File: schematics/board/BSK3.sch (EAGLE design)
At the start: 27 parts

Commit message: Платы подготовлены для Резонита
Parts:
- removed U$14: FS8205A, CanCubeSat:FS8205A
- added FS8205A: FS8205A+, CanCubeSat:FS8205A+
- renumbered U$5 to DS18B20Z, U$8 to L293DD
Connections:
- net BUS-: now also FS8205A.S1; no longer U$14.S1
- net GND: now also FS8205A.S2; no longer U$14.S2
- net HEAT: now also FS8205A.HEAT; no longer U$14.HEAT
- net N$8: now also FS8205A.G1; no longer U$14.G1
- net N$9: now also FS8205A.G2; no longer U$14.G2
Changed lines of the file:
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@@
 </classes>
 <parts>
-<part name="U$5" library="CanCubeSat" deviceset="DS18B20Z" device=""/>
+<part name="DS18B20Z" library="CanCubeSat" deviceset="DS18B20Z" device=""/>
 <part name="U$6" library="CanCubeSat" deviceset="EM_HEAT" device=""/>
 <part name="U$7" library="CanCubeSat" deviceset="EM_HEAT" device=""/>
-<part name="U$8" library="CanCubeSat" deviceset="L293DD" device=""/>
-<part name="U$14" library="CanCubeSat" deviceset="FS8205A" device=""/>
+<part name="L293DD" library="CanCubeSat" deviceset="L293DD" device=""/>
+<part name="FS8205A" library="CanCubeSat" deviceset="FS8205A+" device=""/>
 <part name="R10" library="resistor" library_urn="urn:adsk.eagle:library:348" deviceset="R-US_" device="R0603" package3d_urn="urn:adsk.eagle:package:23555/3" value="10k"/>
 <part name="R11" library="resistor" library_urn="urn:adsk.eagle:library:348" deviceset="R-US_" device="R0603" package3d_urn="urn:adsk.eagle:package:23555/3" value="10k"/>
@@
 </plain>
 <instances>
-<instance part="U$5" gate="G$1" x="119.38" y="160.02" smashed="yes"/>
+<instance part="DS18B20Z" gate="G$1" x="119.38" y="160.02" smashed="yes"/>
 <instance part="U$6" gate="G$1" x="55.88" y="231.14" smashed="yes" rot="R90"/>
 <instance part="U$7" gate="G$1" x="71.12" y="231.14" smashed="yes" rot="R270"/>
-<instance part="U$8" gate="G$1" x="63.5" y="203.2" smashed="yes" rot="R270"/>
-<instance part="U$14" gate="G$1" x="162.56" y="215.9" smashed="yes"/>
+<instance part="L293DD" gate="G$1" x="63.5" y="203.2" smashed="yes" rot="R270"/>
+<instance part="FS8205A" gate="G$1" x="162.56" y="215.9" smashed="yes"/>
 <instance part="R10" gate="G$1" x="157.48" y="233.68" smashed="yes" rot="R270">
 <attribute name="NAME" x="158.9786" y="237.49" size="1.778" layer="95" rot="R270"/>
@@
 </segment>
 <segment>
-<pinref part="U$5" gate="G$1" pin="GND"/>
+<pinref part="DS18B20Z" gate="G$1" pin="GND"/>
 <wire x1="129.54" y1="157.48" x2="137.16" y2="157.48" width="0.1524" layer="91"/>
 <label x="130.556" y="157.48" size="1.778" layer="95"/>
 </segment>
 <segment>
-<pinref part="U$8" gate="G$1" pin="GND"/>
+<pinref part="L293DD" gate="G$1" pin="GND"/>
 <wire x1="50.8" y1="205.74" x2="38.1" y2="205.74" width="0.1524" layer="91"/>
 <label x="39.116" y="205.74" size="1.778" layer="95"/>
 </segment>
 <segment>
-<pinref part="U$14" gate="G$1" pin="S2"/>
+<pinref part="FS8205A" gate="G$1" pin="S2"/>
 <wire x1="175.26" y1="215.9" x2="185.42" y2="215.9" width="0.1524" layer="91"/>
 <label x="180.34" y="215.9" size="1.778" layer="95"/>
@@
 <net name="5V" class="0">
 <segment>
-<pinref part="U$8" gate="G$1" pin="EN1"/>
+<pinref part="L293DD" gate="G$1" pin="EN1"/>
 <wire x1="50.8" y1="213.36" x2="38.1" y2="213.36" width="0.1524" layer="91"/>
 <label x="38.862" y="213.36" size="1.778" layer="95"/>
 </segment>
 <segment>
-<pinref part="U$8" gate="G$1" pin="VS"/>
+<pinref part="L293DD" gate="G$1" pin="VS"/>
 <wire x1="50.8" y1="190.5" x2="38.1" y2="190.5" width="0.1524" layer="91"/>
 <label x="38.862" y="190.5" size="1.778" layer="95"/>
 </segment>
 <segment>
-<pinref part="U$8" gate="G$1" pin="EN2"/>
+<pinref part="L293DD" gate="G$1" pin="EN2"/>
 <wire x1="76.2" y1="190.5" x2="81.28" y2="190.5" width="0.1524" layer="91"/>
 <label x="77.47" y="190.5" size="1.778" layer="95"/>
 </segment>
 <segment>
-<pinref part="U$8" gate="G$1" pin="VSS"/>
+<pinref part="L293DD" gate="G$1" pin="VSS"/>
 <wire x1="76.2" y1="213.36" x2="81.28" y2="213.36" width="0.1524" layer="91"/>
 <label x="77.216" y="213.36" size="1.778" layer="95"/>
@@
 </segment>
 <segment>
-<pinref part="U$5" gate="G$1" pin="VDD"/>
+<pinref part="DS18B20Z" gate="G$1" pin="VDD"/>
 <wire x1="106.68" y1="160.02" x2="99.06" y2="160.02" width="0.1524" layer="91"/>
 <label x="101.6" y="160.02" size="1.778" layer="95"/>
@@
 <net name="1W" class="0">
 <segment>
-<pinref part="U$5" gate="G$1" pin="DQ"/>
+<pinref part="DS18B20Z" gate="G$1" pin="DQ"/>
 <wire x1="106.68" y1="157.48" x2="99.06" y2="157.48" width="0.1524" layer="91"/>
 <label x="101.6" y="157.48" size="1.778" layer="95"/>
@@
 </segment>
 <segment>
-<pinref part="U$8" gate="G$1" pin="IN1"/>
+<pinref part="L293DD" gate="G$1" pin="IN1"/>
 <wire x1="50.8" y1="210.82" x2="38.1" y2="210.82" width="0.1524" layer="91"/>
 <label x="38.862" y="210.82" size="1.778" layer="95"/>
@@
 </segment>
 <segment>
-<pinref part="U$8" gate="G$1" pin="IN2"/>
+<pinref part="L293DD" gate="G$1" pin="IN2"/>
 <wire x1="50.8" y1="193.04" x2="38.1" y2="193.04" width="0.1524" layer="91"/>
 <label x="38.862" y="193.04" size="1.778" layer="95"/>
@@
 </segment>
 <segment>
-<pinref part="U$8" gate="G$1" pin="IN4"/>
+<pinref part="L293DD" gate="G$1" pin="IN4"/>
 <wire x1="76.2" y1="210.82" x2="86.36" y2="210.82" width="0.1524" layer="91"/>
 <label x="76.962" y="210.82" size="1.778" layer="95"/>
@@
 <wire x1="35.56" y1="228.6" x2="30.48" y2="228.6" width="0.1524" layer="91"/>
 <wire x1="30.48" y1="228.6" x2="30.48" y2="208.28" width="0.1524" layer="91"/>
-<pinref part="U$8" gate="G$1" pin="OUT1"/>
+<pinref part="L293DD" gate="G$1" pin="OUT1"/>
 <wire x1="30.48" y1="208.28" x2="50.8" y2="208.28" width="0.1524" layer="91"/>
 <pinref part="LED2" gate="G$1" pin="A"/>
@@
 <segment>
 <wire x1="27.94" y1="246.38" x2="27.94" y2="195.58" width="0.1524" layer="91"/>
-<pinref part="U$8" gate="G$1" pin="OUT2"/>
+<pinref part="L293DD" gate="G$1" pin="OUT2"/>
 <wire x1="27.94" y1="195.58" x2="50.8" y2="195.58" width="0.1524" layer="91"/>
 <pinref part="U$6" gate="G$1" pin="GND"/>
@@
 <segment>
 <wire x1="101.6" y1="246.38" x2="101.6" y2="208.28" width="0.1524" layer="91"/>
-<pinref part="U$8" gate="G$1" pin="OUT4"/>
+<pinref part="L293DD" gate="G$1" pin="OUT4"/>
 <wire x1="101.6" y1="208.28" x2="76.2" y2="208.28" width="0.1524" layer="91"/>
 <pinref part="U$7" gate="G$1" pin="5V"/>
@@
 <net name="BUS-" class="0">
 <segment>
-<pinref part="U$14" gate="G$1" pin="S1"/>
+<pinref part="FS8205A" gate="G$1" pin="S1"/>
 <wire x1="142.24" y1="215.9" x2="149.86" y2="215.9" width="0.1524" layer="91"/>
 <pinref part="R20" gate="G$1" pin="2"/>
@@
 <net name="N$8" class="0">
 <segment>
-<pinref part="U$14" gate="G$1" pin="G1"/>
+<pinref part="FS8205A" gate="G$1" pin="G1"/>
 <pinref part="R10" gate="G$1" pin="2"/>
 <wire x1="157.48" y1="228.6" x2="157.48" y2="226.06" width="0.1524" layer="91"/>
@@
 <pinref part="R11" gate="G$1" pin="2"/>
 <wire x1="167.64" y1="228.6" x2="167.64" y2="226.06" width="0.1524" layer="91"/>
-<pinref part="U$14" gate="G$1" pin="G2"/>
+<pinref part="FS8205A" gate="G$1" pin="G2"/>
 </segment>
 </net>
@@
 <net name="HEAT" class="0">
 <segment>
-<pinref part="U$8" gate="G$1" pin="HEAT"/>
+<pinref part="L293DD" gate="G$1" pin="HEAT"/>
 <wire x1="53.34" y1="200.66" x2="35.56" y2="200.66" width="0.1524" layer="91"/>
 <wire x1="35.56" y1="200.66" x2="35.56" y2="180.34" width="0.1524" layer="91"/>
 <wire x1="35.56" y1="180.34" x2="127" y2="180.34" width="0.1524" layer="91"/>
-<pinref part="U$5" gate="G$1" pin="HEAT"/>
+<pinref part="DS18B20Z" gate="G$1" pin="HEAT"/>
 <wire x1="127" y1="180.34" x2="127" y2="162.56" width="0.1524" layer="91"/>
-<pinref part="U$14" gate="G$1" pin="HEAT"/>
+<pinref part="FS8205A" gate="G$1" pin="HEAT"/>
 <wire x1="162.56" y1="208.28" x2="162.56" y2="180.34" width="0.1524" layer="91"/>
 <wire x1="162.56" y1="180.34" x2="127" y2="180.34" width="0.1524" layer="91"/>

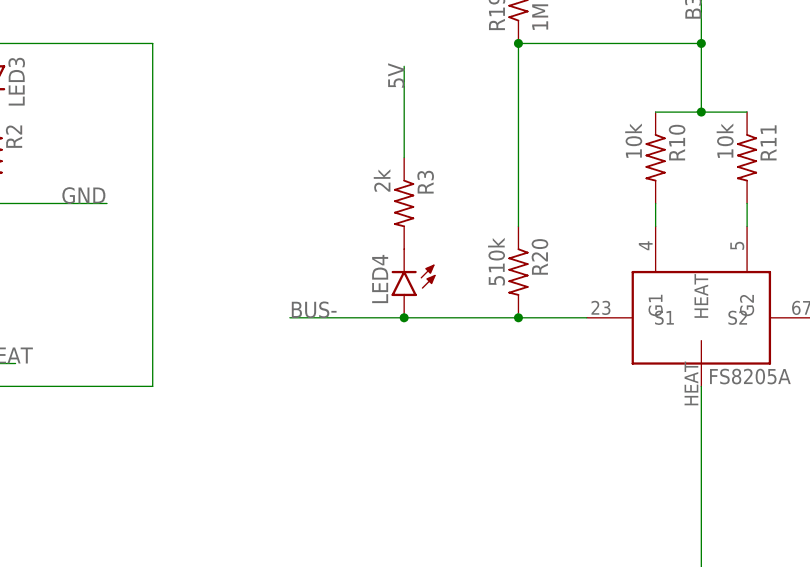
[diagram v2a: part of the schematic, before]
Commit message: Исправлены RADIO и диоды
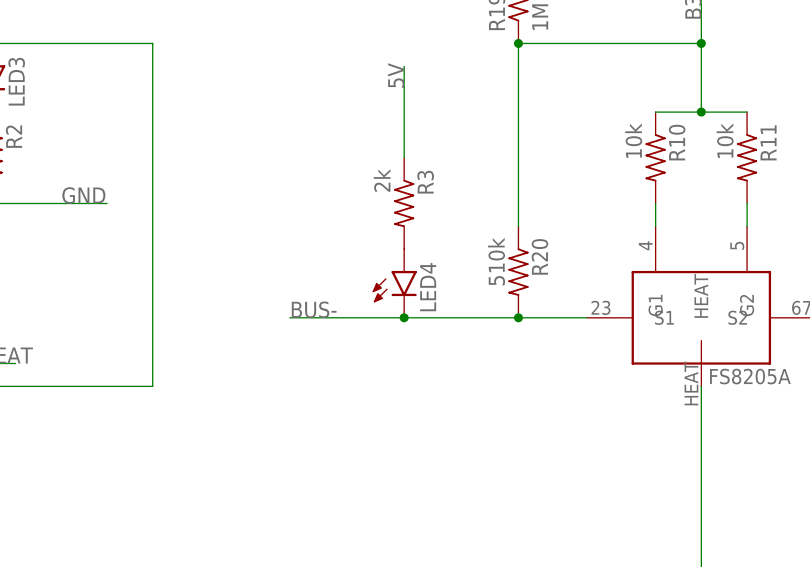
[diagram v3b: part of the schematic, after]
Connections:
- net BUS-: now also LED4.C; no longer LED4.A
- net N$7: now also LED4.A; no longer LED4.C
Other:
- moved on the sheet: LED4
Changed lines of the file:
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@@
 <part name="R2" library="resistor" library_urn="urn:adsk.eagle:library:348" deviceset="R-US_" device="R0603" package3d_urn="urn:adsk.eagle:package:23555/3" value="2k"/>
 <part name="LED3" library="led" library_urn="urn:adsk.eagle:library:259" deviceset="LED" device="CHIPLED_0603" package3d_urn="urn:adsk.eagle:package:15822/2"/>
+<part name="R3" library="resistor" library_urn="urn:adsk.eagle:library:348" deviceset="R-US_" device="R0603" package3d_urn="urn:adsk.eagle:package:23555/3" value="2k"/>
 <part name="LED4" library="led" library_urn="urn:adsk.eagle:library:259" deviceset="LED" device="CHIPLED_0603" package3d_urn="urn:adsk.eagle:package:15822/2"/>
-<part name="R3" library="resistor" library_urn="urn:adsk.eagle:library:348" deviceset="R-US_" device="R0603" package3d_urn="urn:adsk.eagle:package:23555/3" value="2k"/>
 </parts>
 <sheets>
@@
 <attribute name="VALUE" x="89.535" y="239.268" size="1.778" layer="96" rot="R90"/>
 </instance>
-<instance part="LED4" gate="G$1" x="129.54" y="218.44" smashed="yes" rot="R180">
-<attribute name="NAME" x="125.984" y="223.012" size="1.778" layer="95" rot="R270"/>
-<attribute name="VALUE" x="123.825" y="223.012" size="1.778" layer="96" rot="R270"/>
-</instance>
 <instance part="R3" gate="G$1" x="129.54" y="228.6" smashed="yes" rot="R270">
 <attribute name="NAME" x="131.0386" y="232.41" size="1.778" layer="95" rot="R270"/>
 <attribute name="VALUE" x="126.238" y="232.41" size="1.778" layer="96" rot="R270"/>
+</instance>
+<instance part="LED4" gate="G$1" x="129.54" y="220.98" smashed="yes">
+<attribute name="NAME" x="133.096" y="216.408" size="1.778" layer="95" rot="R90"/>
+<attribute name="VALUE" x="135.255" y="216.408" size="1.778" layer="96" rot="R90"/>
 </instance>
 </instances>
@@
 <wire x1="142.24" y1="215.9" x2="149.86" y2="215.9" width="0.1524" layer="91"/>
 <pinref part="R20" gate="G$1" pin="2"/>
-<wire x1="142.24" y1="215.9" x2="129.54" y2="215.9" width="0.1524" layer="91"/>
 <junction x="142.24" y="215.9"/>
 <label x="116.84" y="215.9" size="1.778" layer="95"/>
-<pinref part="LED4" gate="G$1" pin="A"/>
+<wire x1="142.24" y1="215.9" x2="129.54" y2="215.9" width="0.1524" layer="91"/>
+<pinref part="LED4" gate="G$1" pin="C"/>
 <wire x1="129.54" y1="215.9" x2="116.84" y2="215.9" width="0.1524" layer="91"/>
 <junction x="129.54" y="215.9"/>
@@
 <net name="N$7" class="0">
 <segment>
+<pinref part="LED4" gate="G$1" pin="A"/>
 <pinref part="R3" gate="G$1" pin="2"/>
-<pinref part="LED4" gate="G$1" pin="C"/>
-</segment>
-</net>
+</segment>
+</net>

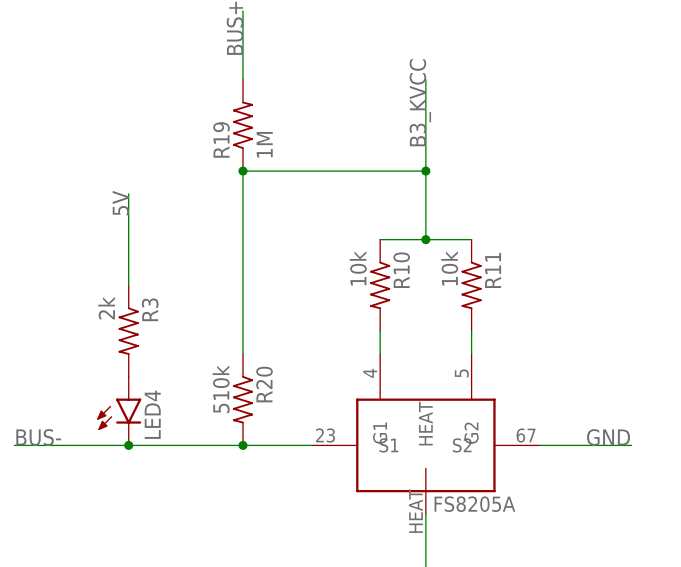
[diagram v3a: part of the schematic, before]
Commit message: Резисторы у FS8205A 100Ом
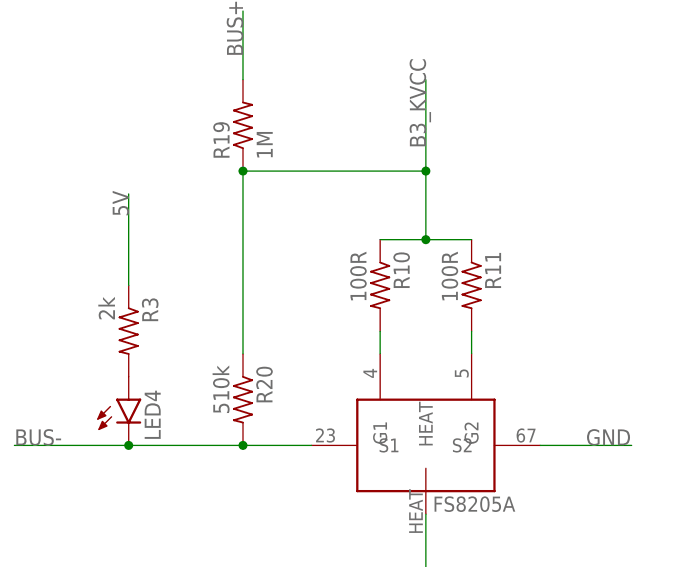
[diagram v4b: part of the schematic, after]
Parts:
- R10, R11: value 10k -> 100R
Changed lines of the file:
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@@
 <part name="L293DD" library="CanCubeSat" deviceset="L293DD" device=""/>
 <part name="FS8205A" library="CanCubeSat" deviceset="FS8205A+" device=""/>
-<part name="R10" library="resistor" library_urn="urn:adsk.eagle:library:348" deviceset="R-US_" device="R0603" package3d_urn="urn:adsk.eagle:package:23555/3" value="10k"/>
-<part name="R11" library="resistor" library_urn="urn:adsk.eagle:library:348" deviceset="R-US_" device="R0603" package3d_urn="urn:adsk.eagle:package:23555/3" value="10k"/>
+<part name="R10" library="resistor" library_urn="urn:adsk.eagle:library:348" deviceset="R-US_" device="R0603" package3d_urn="urn:adsk.eagle:package:23555/3" value="100R"/>
+<part name="R11" library="resistor" library_urn="urn:adsk.eagle:library:348" deviceset="R-US_" device="R0603" package3d_urn="urn:adsk.eagle:package:23555/3" value="100R"/>
 <part name="R19" library="resistor" library_urn="urn:adsk.eagle:library:348" deviceset="R-US_" device="R0603" package3d_urn="urn:adsk.eagle:package:23555/3" value="1M"/>
 <part name="R20" library="resistor" library_urn="urn:adsk.eagle:library:348" deviceset="R-US_" device="R0603" package3d_urn="urn:adsk.eagle:package:23555/3" value="510k"/>
